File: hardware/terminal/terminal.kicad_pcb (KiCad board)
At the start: 2 copper layers, 60 x 40 mm, 26 parts, among them IC1 ATMEGA8-P, J1 RJ45, P1 Prog, P10 CONN_4, P2 RC522, P3 LCD, P4 Keypad, P5 CONN_1, P6 CONN_1, P7 CONN_1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

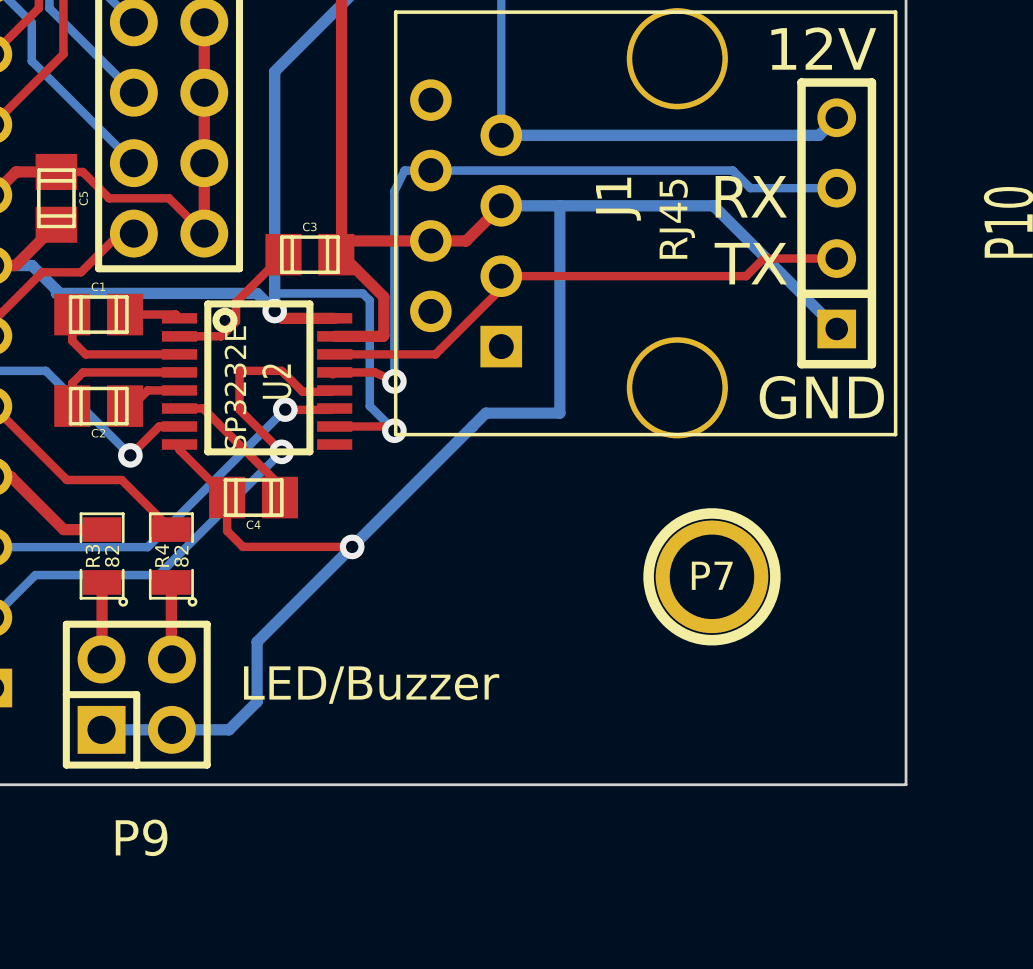
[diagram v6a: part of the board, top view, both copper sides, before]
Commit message: o Add 'playground' area.
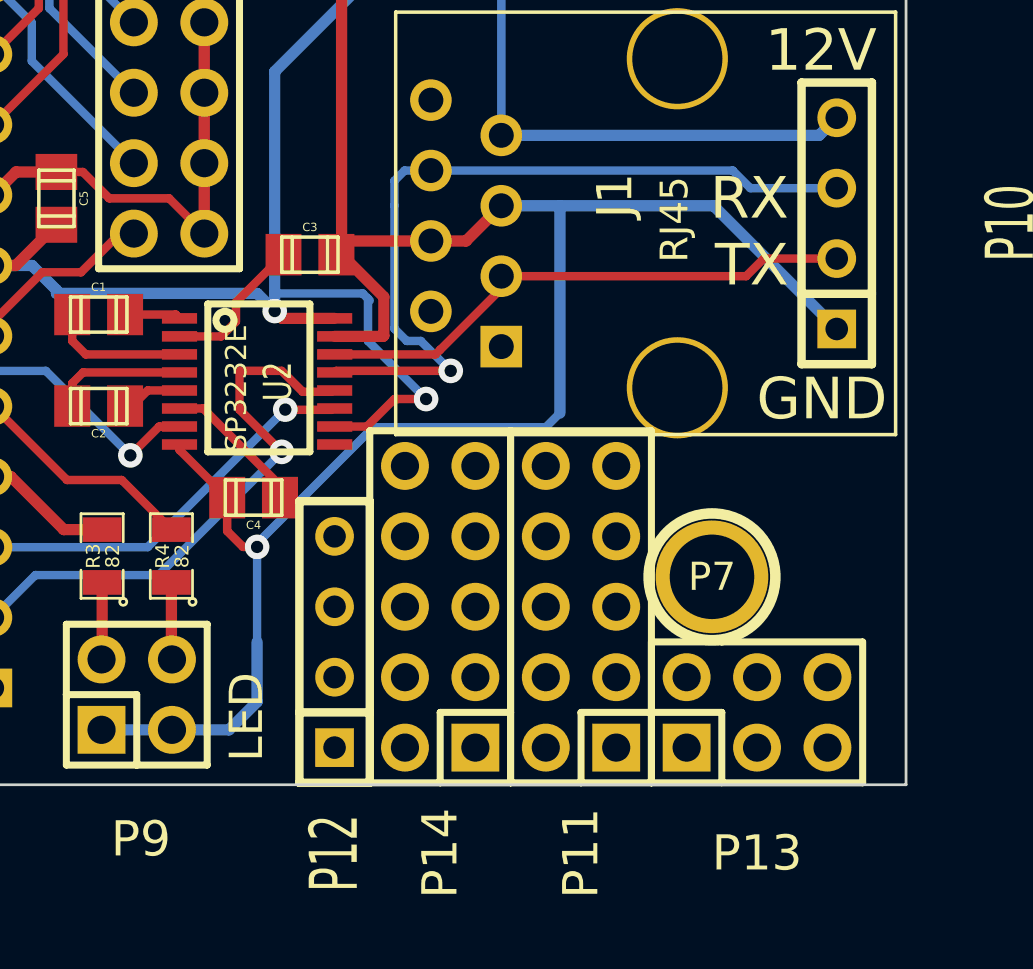
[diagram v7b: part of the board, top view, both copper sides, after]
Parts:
- added P11: CONN_5X2, Pin_Headers:Pin_Header_Straight_2x05, F.Cu at (168.3, 68.6)
- added P12: CONN_4, Connect:SIL-4, F.Cu at (159.4, 69.8)
- added P13: CONN_3X2, Pin_Headers:Pin_Header_Straight_2x03, F.Cu at (174.6, 72.4)
- added P14: CONN_5X2, Pin_Headers:Pin_Header_Straight_2x05, F.Cu at (163.2, 68.6)
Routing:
- net RX-ext: track 25.8 -> 28.6 mm
- net GND: track 180.2 -> 178.9 mm
- net +3.3V: track 122.1 -> 123.0 mm
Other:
- board text added: "LED"
- board text removed: "LED/Buzzer"

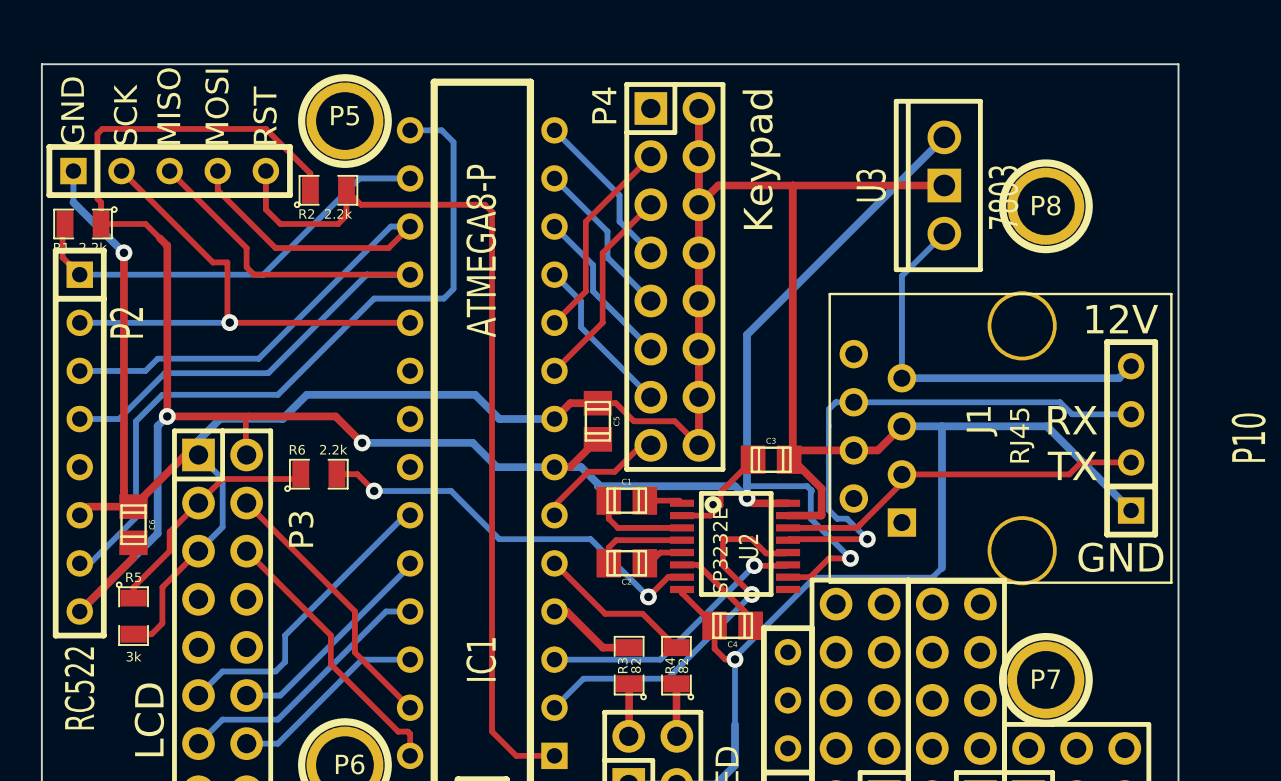
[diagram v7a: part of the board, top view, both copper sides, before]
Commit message: o input voltage label refined.
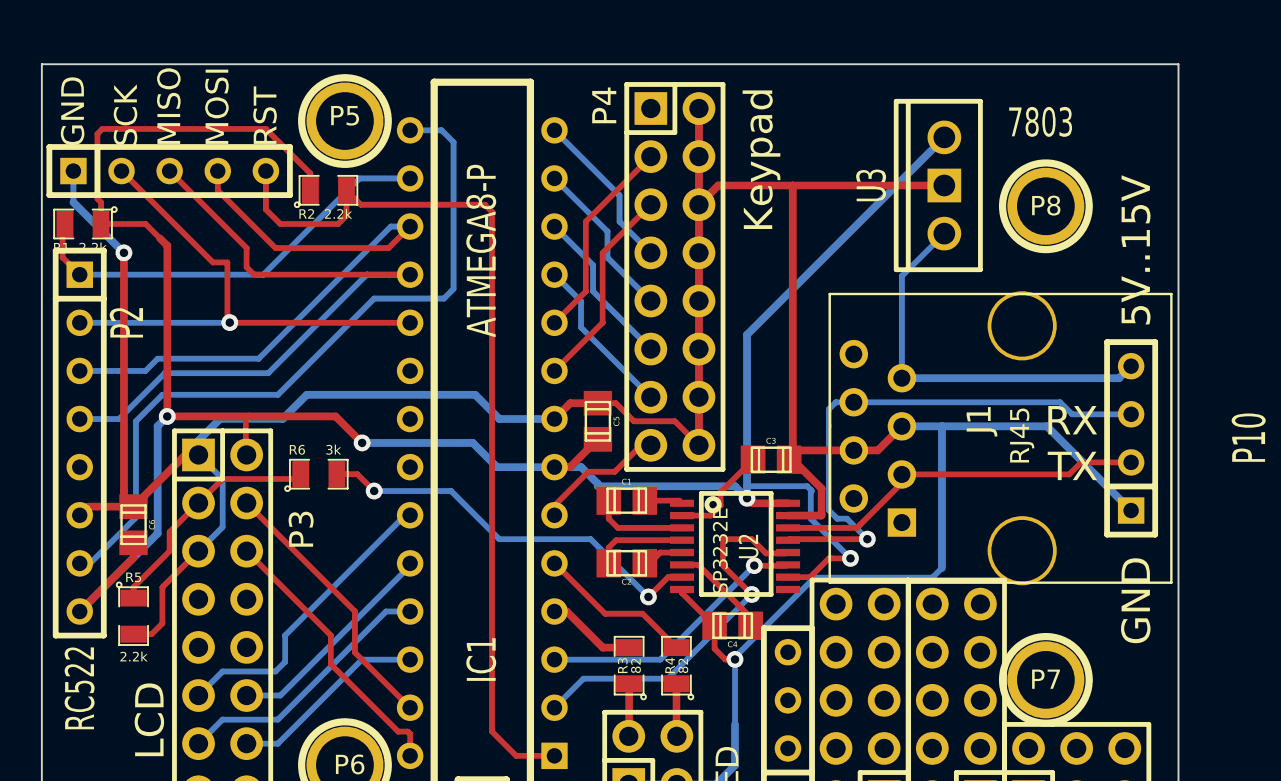
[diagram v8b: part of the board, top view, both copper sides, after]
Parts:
- R5: value 3k -> 2.2k
- R6: value 2.2k -> 3k
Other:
- board text added: "5V..15V"
- board text removed: "12V"
